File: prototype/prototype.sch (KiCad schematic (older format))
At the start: 31 parts, among them P1 CONN_25X2, P2 CONN_25X2, P3 VGACONN, U1 MC68SEC000

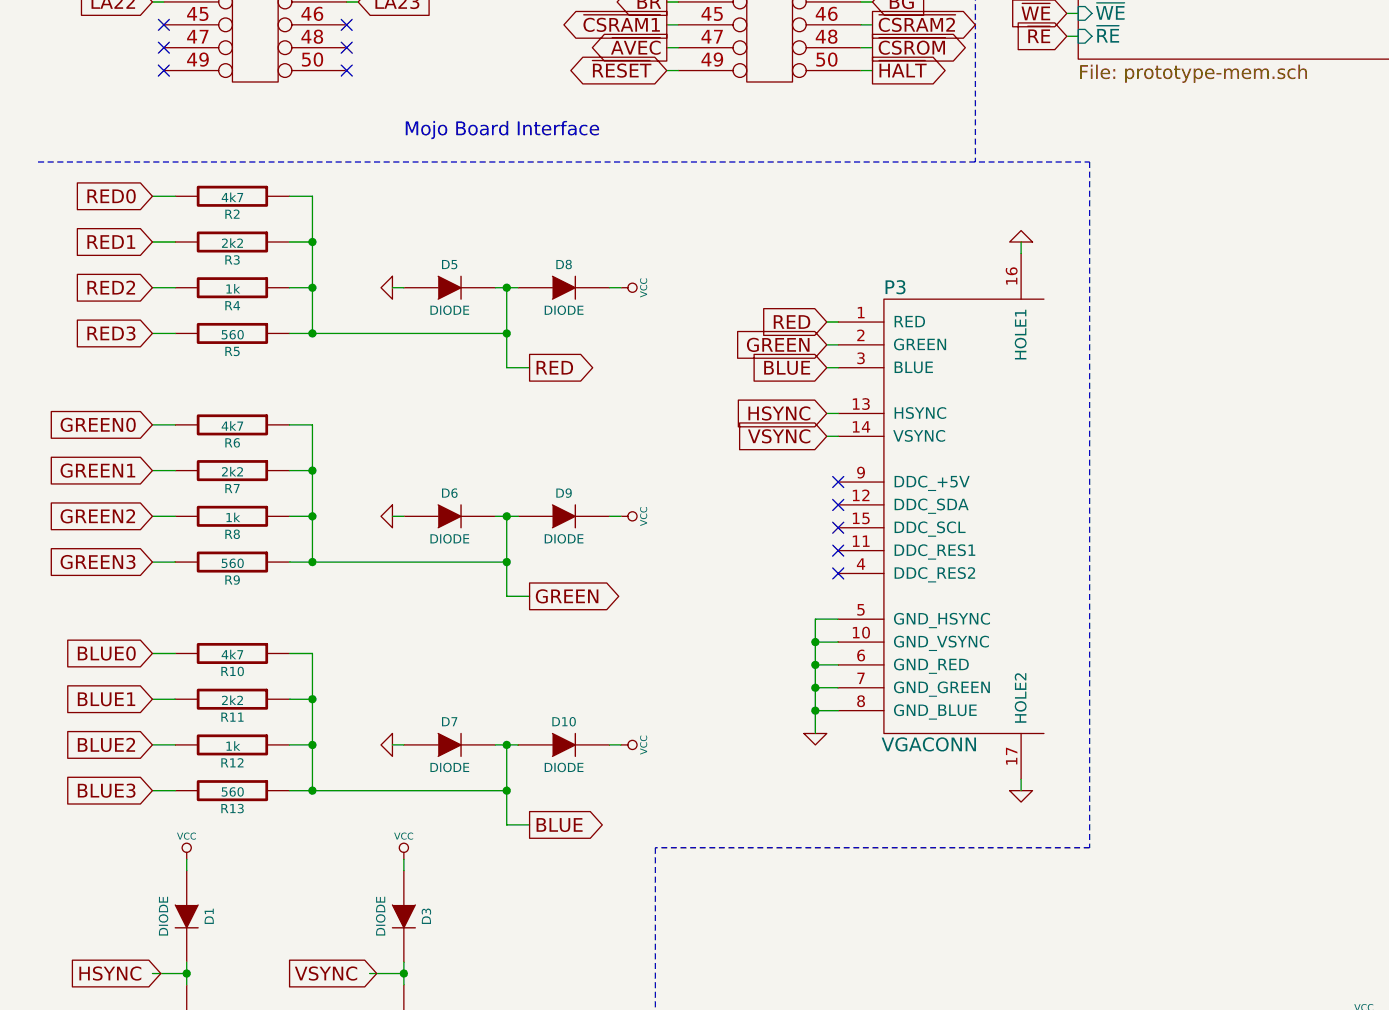
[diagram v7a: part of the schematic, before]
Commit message: Move some bits around for easier PCB layout.
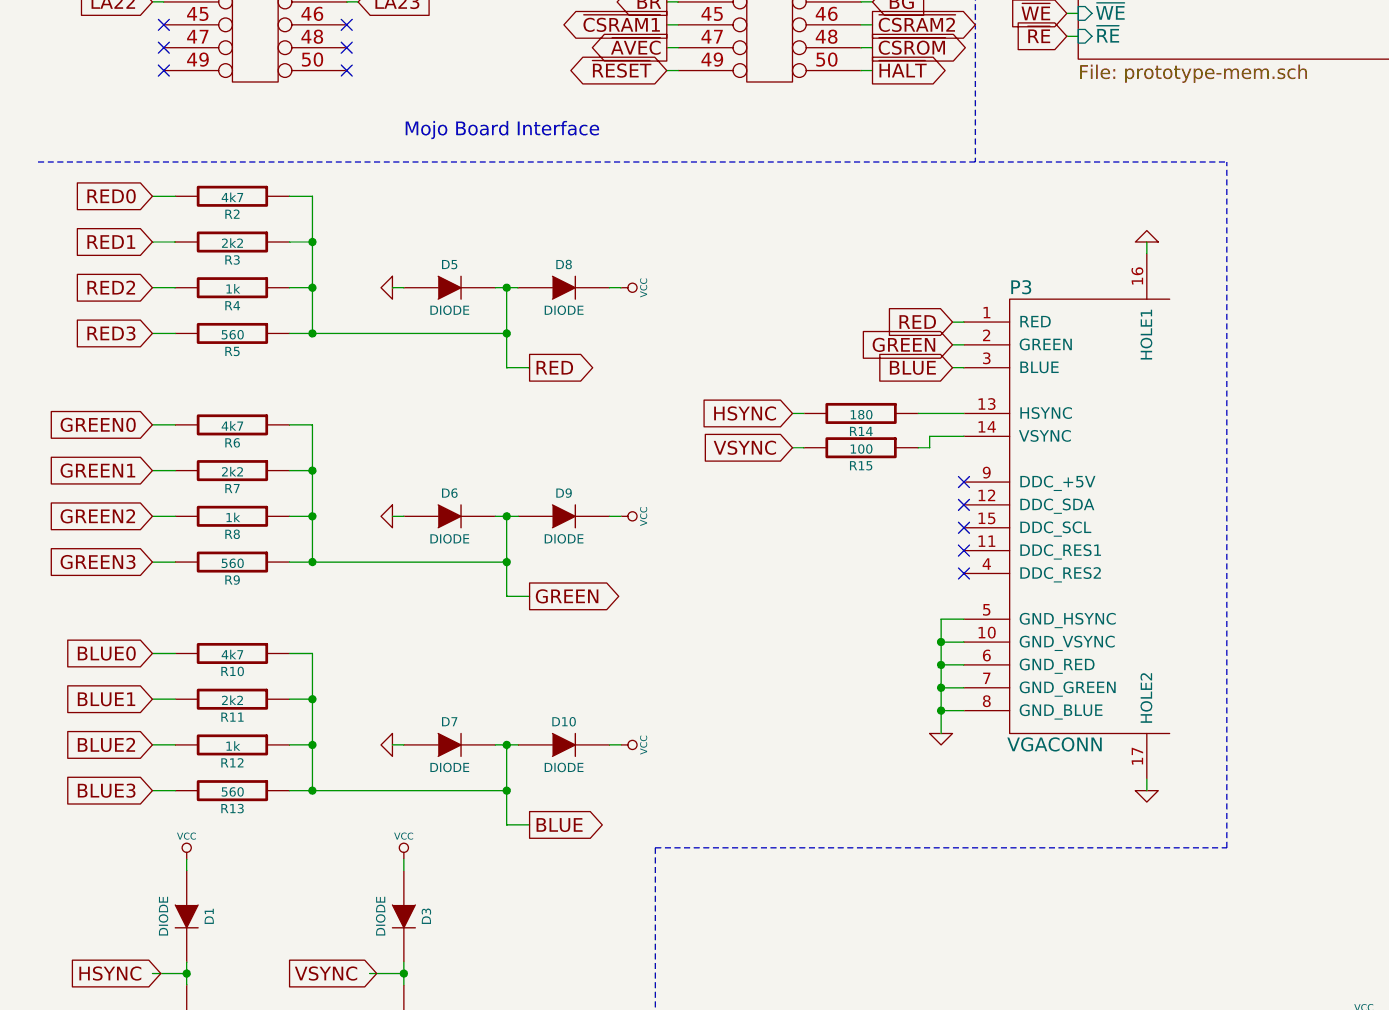
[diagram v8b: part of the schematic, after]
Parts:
- added R14: 180, Resistors_SMD:R_0805_HandSoldering, symbol R
- added R15: 100, Resistors_SMD:R_0805_HandSoldering, symbol R
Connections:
- net HSYNC: now also R14.2; no longer P3.13 (HSYNC)
- net VSYNC: now also R15.2; no longer P3.14 (VSYNC)
- new net: P3.13 (HSYNC), R14.1
- new net: P3.14 (VSYNC), R15.1
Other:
- moved on the sheet: P3
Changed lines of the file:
@@
 L VGACONN P3
 U 1 1 55192E7C
-P 4300 5100
-F 0 "P3" H 4350 6050 60  0000 C CNN
-F 1 "VGACONN" H 4500 4050 60  0000 C CNN
-F 2 "68k-computer:DB_15F-VGA" H 4300 5700 60  0001 C CNN
-F 3 "" H 4300 5700 60  0000 C CNN
-	1    4300 5100
+P 4850 5100
+F 0 "P3" H 4900 6050 60  0000 C CNN
+F 1 "VGACONN" H 5050 4050 60  0000 C CNN
+F 2 "68k-computer:DB_15F-VGA" H 4850 5700 60  0001 C CNN
+F 3 "" H 4850 5700 60  0000 C CNN
+	1    4850 5100
 	1    0    0    -1
 $EndComp
@@
 	4700 600  4700 3600
 Wire Notes Line
-	600  3600 5200 3600
+	600  3600 5800 3600
 Wire Wire Line
 	3350 1300 3400 1300
@@
 Wire Wire Line
 	2200 7600 2200 7650
-Text GLabel 4050 4300 0    60   Input ~ 0
+Text GLabel 4600 4300 0    60   Input ~ 0
 RED
-Text GLabel 4050 4400 0    60   Input ~ 0
+Text GLabel 4600 4400 0    60   Input ~ 0
 GREEN
-Text GLabel 4050 4500 0    60   Input ~ 0
+Text GLabel 4600 4500 0    60   Input ~ 0
 BLUE
-Text GLabel 4050 4700 0    60   Input ~ 0
+Text GLabel 3900 4700 0    60   Input ~ 0
 HSYNC
-Text GLabel 4050 4800 0    60   Input ~ 0
+Text GLabel 3900 4850 0    60   Input ~ 0
 VSYNC
 $Comp
 L GND #PWR018
 U 1 1 55196C8F
-P 4000 6100
-F 0 "#PWR018" H 4000 6100 30  0001 C CNN
-F 1 "GND" H 4000 6030 30  0001 C CNN
-F 2 "" H 4000 6100 60  0000 C CNN
-F 3 "" H 4000 6100 60  0000 C CNN
-	1    4000 6100
-	1    0    0    -1
-$EndComp
-Wire Wire Line
-	4100 5600 4000 5600
-Wire Wire Line
-	4100 5700 4000 5700
-Wire Wire Line
-	4000 5800 4100 5800
-Wire Wire Line
-	4000 5900 4100 5900
-Wire Wire Line
-	4000 6000 4100 6000
+P 4550 6100
+F 0 "#PWR018" H 4550 6100 30  0001 C CNN
+F 1 "GND" H 4550 6030 30  0001 C CNN
+F 2 "" H 4550 6100 60  0000 C CNN
+F 3 "" H 4550 6100 60  0000 C CNN
+	1    4550 6100
+	1    0    0    -1
+$EndComp
+Wire Wire Line
+	4650 5600 4550 5600
+Wire Wire Line
+	4650 5700 4550 5700
+Wire Wire Line
+	4550 5800 4650 5800
+Wire Wire Line
+	4550 5900 4650 5900
+Wire Wire Line
+	4550 6000 4650 6000
 $Comp
 L GND #PWR019
 U 1 1 5519790D
-P 4900 3950
-F 0 "#PWR019" H 4900 3950 30  0001 C CNN
-F 1 "GND" H 4900 3880 30  0001 C CNN
-F 2 "" H 4900 3950 60  0000 C CNN
-F 3 "" H 4900 3950 60  0000 C CNN
-	1    4900 3950
+P 5450 3950
+F 0 "#PWR019" H 5450 3950 30  0001 C CNN
+F 1 "GND" H 5450 3880 30  0001 C CNN
+F 2 "" H 5450 3950 60  0000 C CNN
+F 3 "" H 5450 3950 60  0000 C CNN
+	1    5450 3950
 	-1   0    0    1
 $EndComp
 Wire Wire Line
-	4900 4000 4900 3950
+	5450 4000 5450 3950
 $Comp
 L GND #PWR020
 U 1 1 55197AE6
-P 4900 6350
-F 0 "#PWR020" H 4900 6350 30  0001 C CNN
-F 1 "GND" H 4900 6280 30  0001 C CNN
-F 2 "" H 4900 6350 60  0000 C CNN
-F 3 "" H 4900 6350 60  0000 C CNN
-	1    4900 6350
-	1    0    0    -1
-$EndComp
-Wire Wire Line
-	4900 6300 4900 6350
+P 5450 6350
+F 0 "#PWR020" H 5450 6350 30  0001 C CNN
+F 1 "GND" H 5450 6280 30  0001 C CNN
+F 2 "" H 5450 6350 60  0000 C CNN
+F 3 "" H 5450 6350 60  0000 C CNN
+	1    5450 6350
+	1    0    0    -1
+$EndComp
+Wire Wire Line
+	5450 6300 5450 6350
 Wire Notes Line
-	5200 3600 5200 6600
-Wire Notes Line
-	5200 6600 3300 6600
+	3300 6600 5800 6600
 Wire Notes Line
 	3300 6600 3300 7700
 Wire Wire Line
-	4000 5600 4000 6100
-Connection ~ 4000 5700
-Connection ~ 4000 5800
-Connection ~ 4000 5900
-Connection ~ 4000 6000
-NoConn ~ 4100 5000
-NoConn ~ 4100 5100
-NoConn ~ 4100 5200
-NoConn ~ 4100 5300
-NoConn ~ 4100 5400
-Wire Wire Line
-	4050 4300 4100 4300
-Wire Wire Line
-	4050 4400 4100 4400
-Wire Wire Line
-	4050 4500 4100 4500
-Wire Wire Line
-	4050 4700 4100 4700
-Wire Wire Line
-	4050 4800 4100 4800
+	4550 5600 4550 6100
+Connection ~ 4550 5700
+Connection ~ 4550 5800
+Connection ~ 4550 5900
+Connection ~ 4550 6000
+NoConn ~ 4650 5000
+NoConn ~ 4650 5100
+NoConn ~ 4650 5200
+NoConn ~ 4650 5300
+NoConn ~ 4650 5400
+Wire Wire Line
+	4600 4300 4650 4300
+Wire Wire Line
+	4600 4400 4650 4400
+Wire Wire Line
+	4600 4500 4650 4500
+Wire Wire Line
+	4450 4700 4650 4700
+Wire Wire Line
+	4500 4800 4650 4800
 Text GLabel 7250 3050 2    60   Input ~ 0
 ~CSROM
@@
 Wire Wire Line
 	7200 2600 7250 2600
+$Comp
+L R R14
+U 1 1 551C66AB
+P 4200 4700
+F 0 "R14" V 4280 4700 40  0000 C CNN
+F 1 "180" V 4207 4701 40  0000 C CNN
+F 2 "Resistors_SMD:R_0805_HandSoldering" V 4130 4700 30  0001 C CNN
+F 3 "" H 4200 4700 30  0000 C CNN
+	1    4200 4700
+	0    1    1    0
+$EndComp
+$Comp
+L R R15
+U 1 1 551C678E
+P 4200 4850
+F 0 "R15" V 4280 4850 40  0000 C CNN
+F 1 "100" V 4207 4851 40  0000 C CNN
+F 2 "Resistors_SMD:R_0805_HandSoldering" V 4130 4850 30  0001 C CNN
+F 3 "" H 4200 4850 30  0000 C CNN
+	1    4200 4850
+	0    1    1    0
+$EndComp
+Wire Notes Line
+	5800 6600 5800 3600
+Wire Wire Line
+	3900 4850 3950 4850
+Wire Wire Line
+	3900 4700 3950 4700
+Wire Wire Line
+	4450 4850 4500 4850
+Wire Wire Line
+	4500 4850 4500 4800
 $EndSCHEMATC
